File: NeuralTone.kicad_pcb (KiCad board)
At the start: 2 copper layers, 90 parts, among them J1 Power Port (5V@3A), J2 Guitar, J3 Headphone, J4 USB Port, J5 Line Out, J6 TF-01A, J7 RPi CM4Lite Compatible, J8 RPi CM4Lite Compatible, SW1 SW_Push, U1 MCP6022, U2 LDLN025M33R, U3 LDLN025M33R, U4 AP2151, U5 NAU8814YG, Y1 DSB211SDN 26MHz

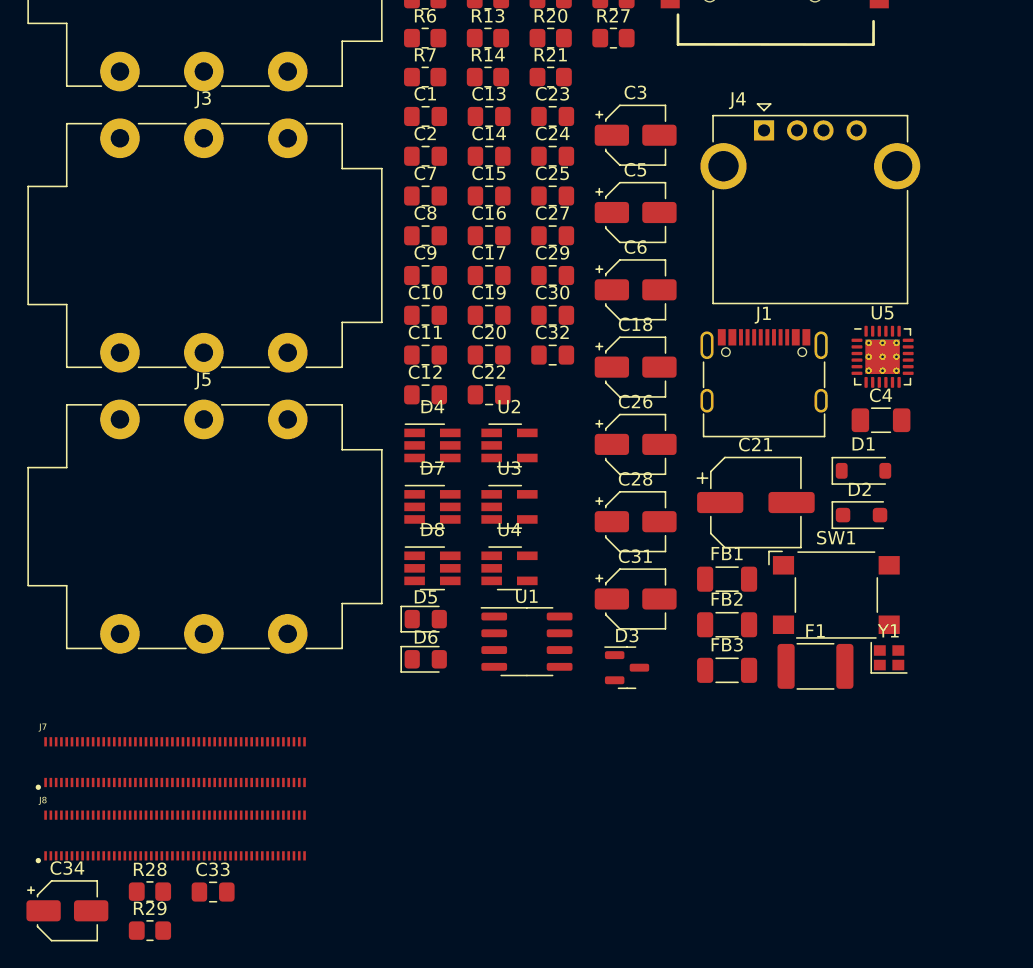
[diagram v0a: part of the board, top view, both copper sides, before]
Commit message: better decoupling strategy
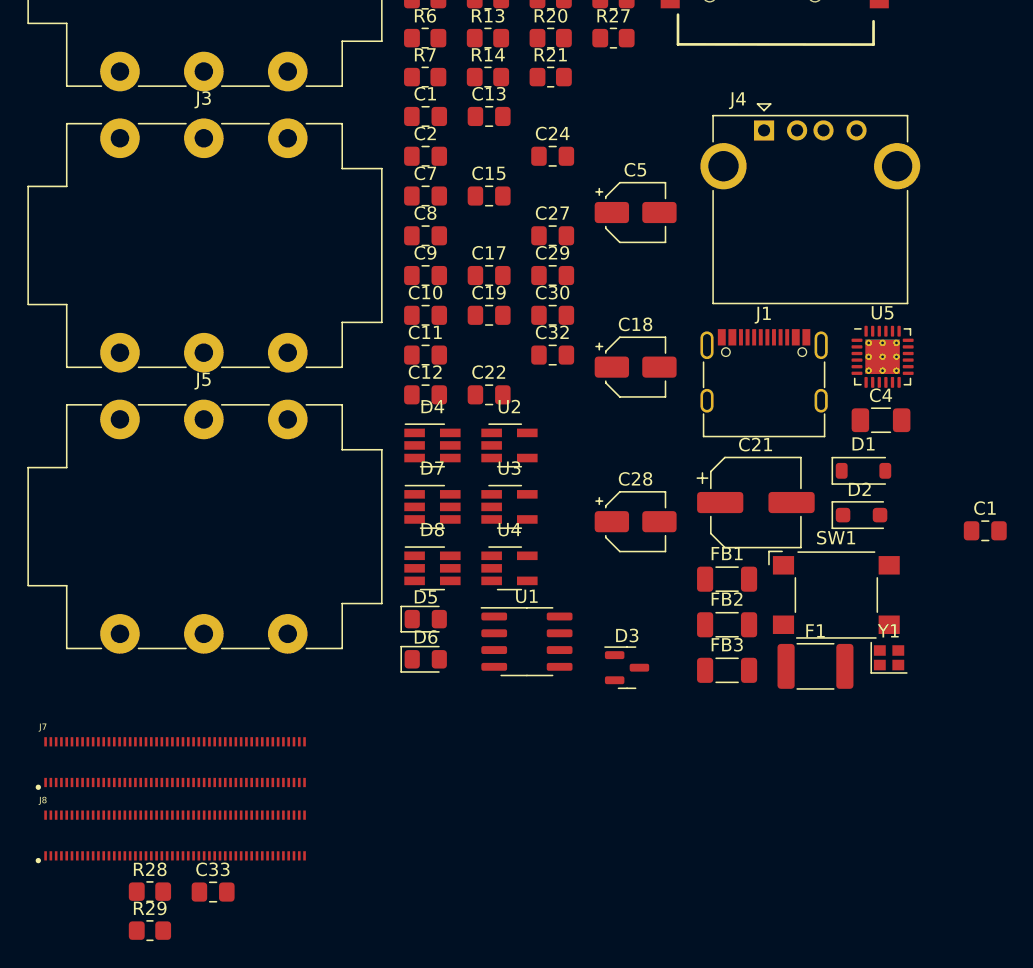
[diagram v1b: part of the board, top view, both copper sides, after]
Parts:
- removed C14, C16, C20, C23, C25: 100n, Capacitor_SMD:C_0805_2012Metric_Pad1.18x1.45mm_HandSolder
- removed C26, C31: 10u, Capacitor_SMD:CP_Elec_4x5.4
- removed C3, C34, C6: 4.7u, Capacitor_SMD:CP_Elec_4x5.4
- added C1: 4.7u, Capacitor_SMD:C_0805_2012Metric_Pad1.18x1.45mm_HandSolder, F.Cu at (186.9, 106.7)
- C1: value 10n -> 4.7u
- C10, C11, C12, C9: value 1u -> 4.7u
- C2: value 100n -> 4.7u
- C27, C30, C32, C33, C7, C8: value 100n -> 470n
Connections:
- C1 pad 1: Net-(D2-K) -> +5V
- C32 pad 1: Net-(J6-CLK) -> +3V3

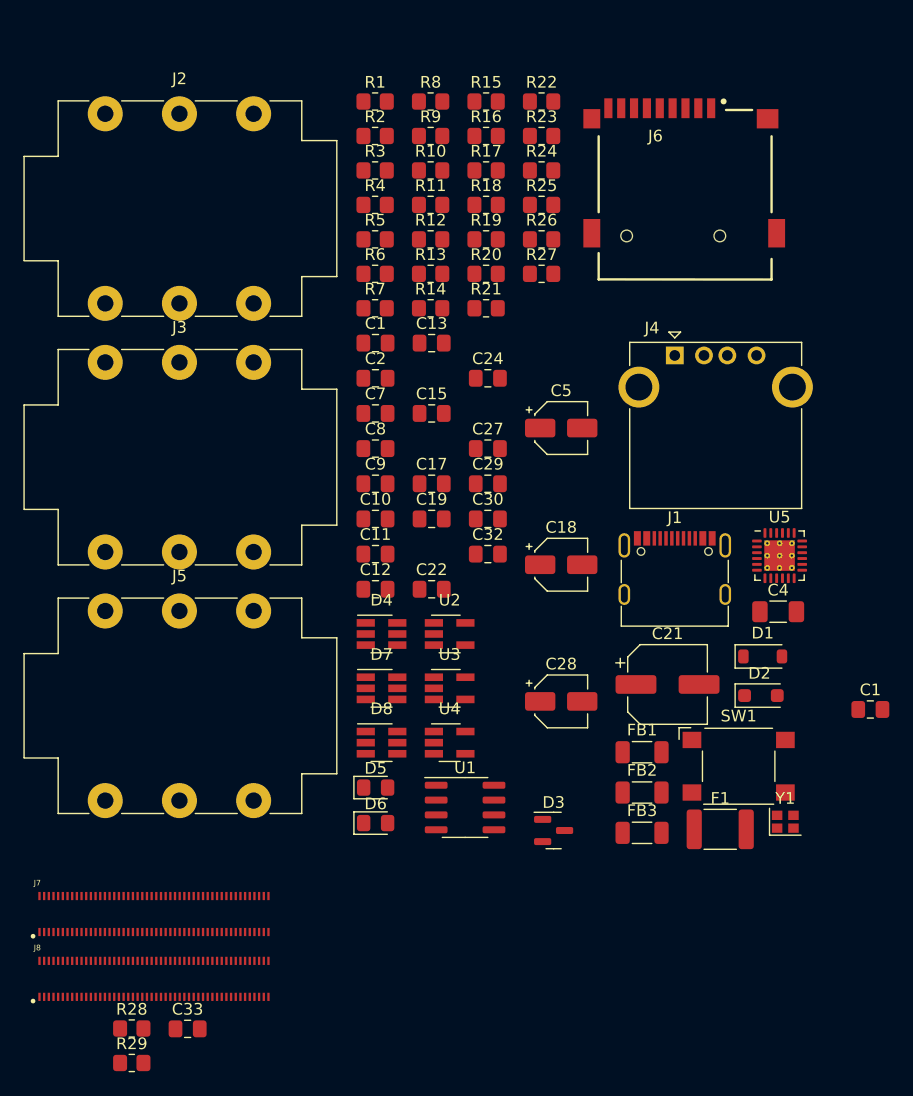
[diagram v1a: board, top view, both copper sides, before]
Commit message: update to a proper USB PD chip
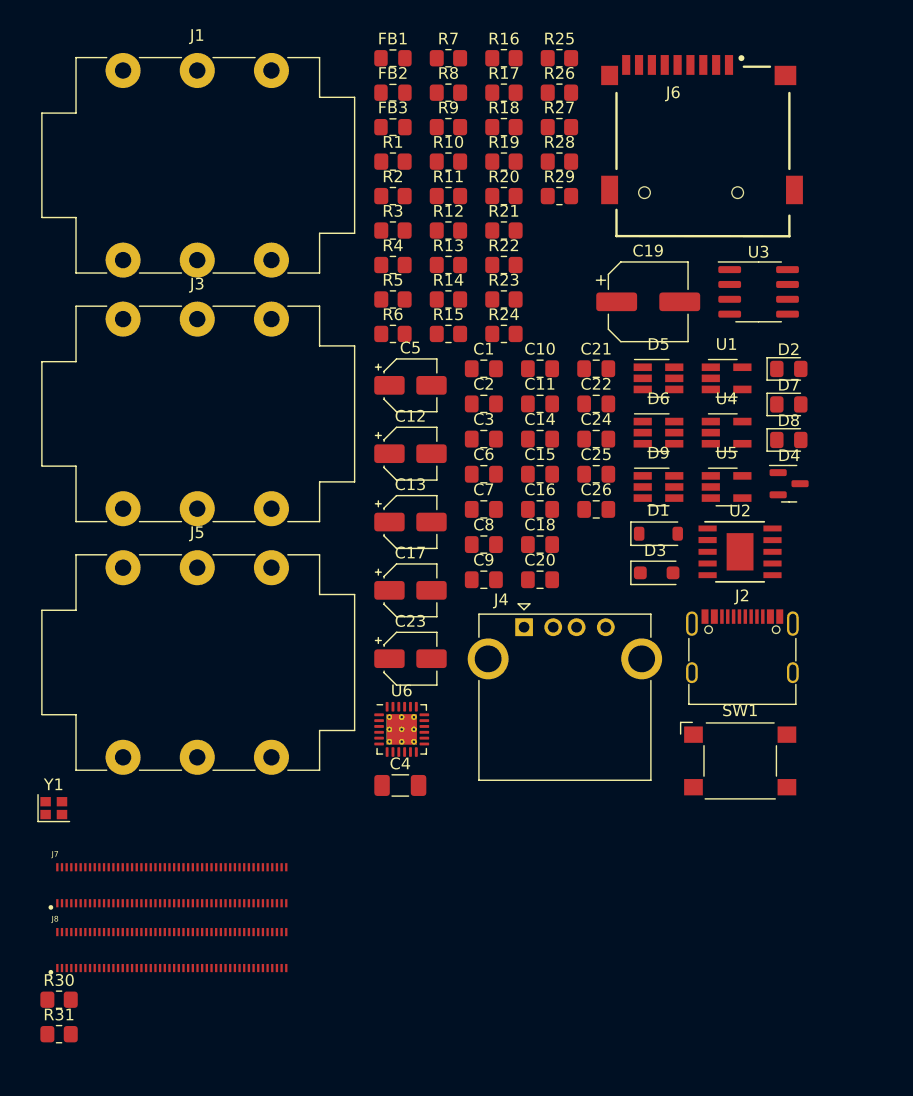
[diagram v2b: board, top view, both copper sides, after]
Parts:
- removed the C1 at (186.9, 106.7)
- removed the C1 at (144.6, 75.3)
- removed C27, C30, C32, C33: 470n, Capacitor_SMD:C_0805_2012Metric_Pad1.18x1.45mm_HandSolder
- removed C28: 10u, Capacitor_SMD:CP_Elec_4x5.4
- removed C29: 100p, Capacitor_SMD:C_0805_2012Metric_Pad1.18x1.45mm_HandSolder
- removed F1: 1812L300, Fuse:Fuse_1812_4532Metric_Pad1.30x3.40mm_HandSolder
- added C1: 1u, Capacitor_SMD:C_0805_2012Metric_Pad1.18x1.45mm_HandSolder, F.Cu at (153.8, 77.5)
- added C14: 4.7u, Capacitor_SMD:C_0805_2012Metric_Pad1.18x1.45mm_HandSolder, F.Cu at (158.6, 83.5)
- added C16: 100p, Capacitor_SMD:C_0805_2012Metric_Pad1.18x1.45mm_HandSolder, F.Cu at (158.6, 89.6)
- added C20: 4.7u, Capacitor_SMD:C_0805_2012Metric_Pad1.18x1.45mm_HandSolder, F.Cu at (158.6, 95.6)
- added C23: 4.7u, Capacitor_SMD:CP_Elec_4x5.4, F.Cu at (147.6, 102.3)
- added C25: 470n, Capacitor_SMD:C_0805_2012Metric_Pad1.18x1.45mm_HandSolder, F.Cu at (163.5, 86.5)
- added C26: 4.7u, Capacitor_SMD:C_0805_2012Metric_Pad1.18x1.45mm_HandSolder, F.Cu at (163.5, 89.6)
- added C3: 1u, Capacitor_SMD:C_0805_2012Metric_Pad1.18x1.45mm_HandSolder, F.Cu at (153.8, 83.5)
- added C6: 4.7u, Capacitor_SMD:C_0805_2012Metric_Pad1.18x1.45mm_HandSolder, F.Cu at (153.8, 86.5)
- added D9: PESD3V3S4UD, Package_TO_SOT_SMD:SOT-23-6_Handsoldering, F.Cu at (168.8, 87.6)
- added R30: 330, Resistor_SMD:R_0805_2012Metric_Pad1.20x1.40mm_HandSolder, F.Cu at (117.5, 131.5)
- added R31: 330, Resistor_SMD:R_0805_2012Metric_Pad1.20x1.40mm_HandSolder, F.Cu at (117.5, 134.5)
- added U6: NAU8814YG, Package_DFN_QFN:QFN-24-1EP_4x4mm_P0.5mm_EP2.6x2.6mm_ThermalVias, F.Cu at (146.8, 108.4)
- C10, C11: value 4.7u -> 10n
- C12, C13: value 4.7u -> 22u; footprint Capacitor_SMD:C_0805_2012Metric_Pad1.18x1.45mm_HandSolder -> Capacitor_SMD:CP_Elec_4x5.4
- C17: value 100p -> 22u; footprint Capacitor_SMD:C_0805_2012Metric_Pad1.18x1.45mm_HandSolder -> Capacitor_SMD:CP_Elec_4x5.4
- C18: value 10u -> 4.7u; footprint Capacitor_SMD:CP_Elec_4x5.4 -> Capacitor_SMD:C_0805_2012Metric_Pad1.18x1.45mm_HandSolder
- C19: value 4.7u -> 150u; footprint Capacitor_SMD:C_0805_2012Metric_Pad1.18x1.45mm_HandSolder -> Capacitor_SMD:CP_Elec_6.3x5.8
- C21: value 100u -> 4.7u; footprint Capacitor_SMD:CP_Elec_6.3x7.7 -> Capacitor_SMD:C_0805_2012Metric_Pad1.18x1.45mm_HandSolder
- C24: value 4.7u -> 100p
- C4: value 150n -> 100n
- C7: value 470n -> 1u
- C9: value 4.7u -> 470n
- D2: value SMF6.0A -> LED_Small; footprint Diode_SMD:D_SOD-123F -> LED_SMD:LED_0805_2012Metric_Pad1.15x1.40mm_HandSolder
- D3: value PESD5V2S2UT -> SMF5.0A; footprint Package_TO_SOT_SMD:SOT-23 -> Diode_SMD:D_SOD-123F
- D4: value PESD3V3S4UD -> PESD5V2S2UT; footprint Package_TO_SOT_SMD:SOT-23-6_Handsoldering -> Package_TO_SOT_SMD:SOT-23
- D5: value LED_Small -> USBLC6-2P6; footprint LED_SMD:LED_0805_2012Metric_Pad1.15x1.40mm_HandSolder -> Package_TO_SOT_SMD:SOT-23-6_Handsoldering
- D6: value LED_Small -> PESD3V3S4UD; footprint LED_SMD:LED_0805_2012Metric_Pad1.15x1.40mm_HandSolder -> Package_TO_SOT_SMD:SOT-23-6_Handsoldering
- D7: value PESD3V3S4UD -> LED_Small; footprint Package_TO_SOT_SMD:SOT-23-6_Handsoldering -> LED_SMD:LED_0805_2012Metric_Pad1.15x1.40mm_HandSolder
- D8: value USBLC6-2P6 -> LED_Small; footprint Package_TO_SOT_SMD:SOT-23-6_Handsoldering -> LED_SMD:LED_0805_2012Metric_Pad1.15x1.40mm_HandSolder
- FB1: value BLM31PG121SN1L -> BLM21PG220SN1; footprint Inductor_SMD:L_1206_3216Metric_Pad1.22x1.90mm_HandSolder -> Inductor_SMD:L_0805_2012Metric_Pad1.15x1.40mm_HandSolder
- FB2, FB3: value BLM31PG121SN1L -> BLM21AG102SN1; footprint Inductor_SMD:L_1206_3216Metric_Pad1.22x1.90mm_HandSolder -> Inductor_SMD:L_0805_2012Metric_Pad1.15x1.40mm_HandSolder
- J1: value Power Port (5V@3A) -> Guitar; footprint Connector_USB:USB_C_Receptacle_G-Switch_GT-USB-7010ASV -> Connector_Audio:Jack_6.35mm_Neutrik_NMJ6HCD2_Horizontal
- J2: value Guitar -> 5V@3A; footprint Connector_Audio:Jack_6.35mm_Neutrik_NMJ6HCD2_Horizontal -> Connector_USB:USB_C_Receptacle_G-Switch_GT-USB-7010ASV
- J3: value Headphone -> Headphones
- R1: value 1.8k -> 1k
- R11: value 10k -> 2.2M
- R14, R15, R20: value 22 -> 10k
- R18, R19: value 10k -> 22
- R2: value 3.9k -> 10k
- R21: value 330 -> 10k
- R23, R26: value 22 -> 1k
- R24, R28, R29: value 330 -> 22
- R3: value 5.1k -> 10k
- R4: value 100 -> 10k
- R5: value 5.1k -> 1.8k
- R6: value 2.2M -> 3.9k
- R7: value 10k -> 100
- R9: value 10k -> 1k
- U1: value MCP6022 -> LDLN025M33R; footprint Package_SO:SOIC-8_3.9x4.9mm_P1.27mm -> Package_TO_SOT_SMD:SOT-23-5_HandSoldering
- U2: value LDLN025M33R -> CH224K; footprint Package_TO_SOT_SMD:SOT-23-5_HandSoldering -> NeuralTone:CH224K
- U3: value LDLN025M33R -> MCP6022; footprint Package_TO_SOT_SMD:SOT-23-5_HandSoldering -> Package_SO:SOIC-8_3.9x4.9mm_P1.27mm
- U4: value AP2151 -> LDLN025M33R
- U5: value NAU8814YG -> AP2151; footprint Package_DFN_QFN:QFN-24-1EP_4x4mm_P0.5mm_EP2.6x2.6mm_ThermalVias -> Package_TO_SOT_SMD:SOT-23-5_HandSoldering
- moved R28 82.7 mm to (160.3, 59.8)
- moved R29 82.7 mm to (160.3, 62.7)
- moved J2 71.8 mm to (176.0, 102.5)
- moved J1 64.4 mm to (123.0, 52.0)
- moved FB3 64.1 mm to (146.1, 56.8)
- moved FB2 63.6 mm to (146.1, 53.9)
- moved FB1 63.1 mm to (146.1, 50.9)
- moved Y1 62.6 mm to (117.0, 115.1)
- moved D8 43.4 mm to (179.9, 83.6)
- moved U3 43.0 mm to (177.4, 70.9)
- moved U1 43.0 mm to (174.6, 78.3)
- moved D5 42.6 mm to (168.8, 78.3)
- moved D7 42.5 mm to (179.9, 80.6)
- moved D6 41.3 mm to (168.8, 83.0)
- moved D4 37.2 mm to (180.0, 87.4)
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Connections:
- C10 pad 1: +3V3A_C -> /VBUS
- C13 pad 1: +3V3A_C -> +5V
- C17 pad 1: Net-(C17-Pad1) -> /HEADPHONES
- C17 pad 2: GND -> Net-(C16-Pad1)
- C18 pad 1: /HEADPHONE -> GND
- C18 pad 2: Net-(C17-Pad1) -> Net-(U6-VREF)
- C19 pad 1: GND -> Net-(J4-VBUS)
- C19 pad 2: Net-(U5-VREF) -> GND
- C2 pad 1: +5V -> +3V3A_B
- C21 pad 1: Net-(J4-VBUS) -> +3V3
- C22 pad 1: +3V3 -> +5V
- C24 pad 1: +3V3 -> GND
- C24 pad 2: GND -> Net-(C23-Pad2)
- C4 pad 2: Net-(U1B-+) -> Net-(U3B-+)
- C5 pad 1: Net-(U1B--) -> Net-(U3B--)
- C7 pad 1: GND -> +5V
- C7 pad 2: Net-(U1A-+) -> GND
- C8 pad 2: +3V3A_B -> Net-(U3A-+)
- C9 pad 1: +3V3A_B -> GND
- C9 pad 2: GND -> +3V3A_B
- D2 pad 2: GND -> Net-(D2-A)
- D3 pad 1: Net-(C17-Pad1) -> /VBUS
- D3 pad 2: Net-(C28-Pad2) -> GND
- D4 pad 1: Net-(J6-DAT2) -> Net-(C16-Pad1)
- D4 pad 2: GND -> Net-(C23-Pad2)
- D4 pad 3: Net-(J6-DAT3/CD) -> GND
- D5 pad 1: GND -> USBD+
- D5 pad 2: Net-(D5-A) -> GND
- D6 pad 1: GND -> Net-(J6-DAT2)
- D6 pad 2: Net-(D6-A) -> GND
- D7 pad 1: Net-(J6-CLK) -> GND
- D7 pad 2: GND -> Net-(D7-A)
- D8 pad 1: USBD+ -> GND
- D8 pad 2: GND -> Net-(D8-A)
- FB1 pad 1: Net-(D2-K) -> /VBUS
- FB2 pad 1: Net-(C17-Pad1) -> Net-(C16-Pad1)
- FB3 pad 1: Net-(C28-Pad2) -> Net-(C23-Pad2)
- R1 pad 1: Net-(J2-PadT) -> /VBUS
- R1 pad 2: Net-(D1-A) -> /VDD
- R10 pad 2: Net-(U1A-+) -> Net-(C5-Pad2)
- R11 pad 1: +5V -> Net-(U3A--)
- R11 pad 2: Net-(U2-EN) -> Net-(U3B-+)
- R12 pad 1: +5V -> Net-(U3A-+)
- R12 pad 2: Net-(U3-EN) -> +3V3A_B
- R14 pad 1: I2S_DOUT -> GND
- R14 pad 2: Net-(U5-ADCOUT) -> Net-(U3A-+)
- R15 pad 1: I2S_DIN -> +5V
- R15 pad 2: Net-(U5-DACIN) -> Net-(U5-EN)
- R16 pad 1: I2S_LRCK -> I2S_DOUT
- R16 pad 2: Net-(U5-FS) -> Net-(U6-ADCOUT)
- R17 pad 1: I2S_BCK -> I2S_DIN
- R17 pad 2: Net-(U5-BCLK) -> Net-(U6-DACIN)
- R18 pad 1: Net-(U5-MODE) -> I2S_LRCK
- R18 pad 2: GND -> Net-(U6-FS)
- R19 pad 1: GND -> I2S_BCK
- R19 pad 2: Net-(U5-CSb/GPIO) -> Net-(U6-BCLK)
- R2 pad 1: Net-(D1-A) -> +5V
- R2 pad 2: Net-(C4-Pad1) -> Net-(U1-EN)
- R20 pad 1: SD_DAT2 -> Net-(U6-MODE)
- R20 pad 2: Net-(J6-DAT2) -> GND
- R21 pad 1: LED_STAT_1 -> GND
- R21 pad 2: Net-(D5-A) -> Net-(U6-CSb/GPIO)
- R22 pad 1: SD_DAT3 -> SD_DAT2
- R22 pad 2: Net-(J6-DAT3/CD) -> Net-(J6-DAT2)
- R23 pad 1: SD_CMD -> LED_STAT_1
- R23 pad 2: Net-(J6-CMD) -> Net-(D7-A)
- R24 pad 1: LED_STAT_2 -> SD_DAT3
- R24 pad 2: Net-(D6-A) -> Net-(J6-DAT3/CD)
- R25 pad 1: SD_CLK -> SD_CMD
- R25 pad 2: Net-(J6-CLK) -> Net-(J6-CMD)
- R26 pad 1: SD_DAT0 -> LED_STAT_2
- R26 pad 2: Net-(J6-DAT0) -> Net-(D8-A)
- R27 pad 1: SD_DAT1 -> SD_CLK
- R27 pad 2: Net-(J6-DAT1) -> Net-(J6-CLK)
- R28 pad 1: I2C_SCL -> SD_DAT0
- R28 pad 2: Net-(J7-GPIO3) -> Net-(J6-DAT0)
- R29 pad 1: I2C_SDA -> SD_DAT1
- R29 pad 2: Net-(J7-GPIO2) -> Net-(J6-DAT1)
- R3 pad 1: Net-(J1-CC1) -> /VBUS
- R3 pad 2: GND -> Net-(U2-VBUS)
- R4 pad 1: Net-(C5-Pad2) -> Net-(U2-CFG1)
- R4 pad 2: CODEC_AUX -> /VDD
- R5 pad 1: Net-(J1-CC2) -> Net-(J1-PadT)
- R5 pad 2: GND -> Net-(D1-A)
- R6 pad 1: Net-(C4-Pad1) -> Net-(D1-A)
- R6 pad 2: GND -> Net-(C4-Pad1)
- R7 pad 1: GND -> Net-(C5-Pad2)
- R7 pad 2: Net-(C5-Pad2) -> CODEC_AUX
- R8 pad 1: Net-(U1A--) -> Net-(C4-Pad1)
- R8 pad 2: Net-(U1B-+) -> GND
- R9 pad 1: Net-(U1A-+) -> Net-(D2-A)
- R9 pad 2: +3V3A_B -> /VDD
- U1 pad 1: Net-(U1A--) -> +5V
- U1 pad 2: Net-(U1A--) -> GND
- U1 pad 3: Net-(U1A-+) -> Net-(U1-EN)
- U1 pad 4: GND -> unconnected-(U1-NC-Pad4)
- U1 pad 5: Net-(U1B-+) -> +3V3A_B
- U2 pad 1: +5V -> /VDD
- U2 pad 2: GND -> unconnected-(U2-CFG2-Pad2)
- U2 pad 3: Net-(U2-EN) -> unconnected-(U2-CFG3-Pad3)
- U2 pad 4: unconnected-(U2-NC-Pad4) -> Net-(U2-DP)
- U2 pad 5: +3V3A_B -> Net-(U2-DM)
- U3 pad 1: +5V -> Net-(U3A--)
- U3 pad 2: GND -> Net-(U3A--)
- U3 pad 3: Net-(U3-EN) -> Net-(U3A-+)
- U3 pad 4: unconnected-(U3-NC-Pad4) -> GND
- U3 pad 5: +3V3A_C -> Net-(U3B-+)
- U4 pad 1: Net-(J4-VBUS) -> +5V
- U4 pad 3: unconnected-(U4-~{FLG}-Pad3) -> Net-(U4-EN)
- U4 pad 4: Net-(U4-EN) -> unconnected-(U4-NC-Pad4)
- U4 pad 5: +5V -> +3V3A_C
- U5 pad 1: unconnected-(U5-MICBIAS-Pad1) -> Net-(J4-VBUS)
- U5 pad 2: +3V3A_C -> GND
- U5 pad 3: GND -> unconnected-(U5-~{FLG}-Pad3)
- U5 pad 4: +3V3 -> Net-(U5-EN)
- U5 pad 5: +3V3 -> +5V

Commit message: cleanup and lcsc part numbers
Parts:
- removed FB3: BLM21AG102SN1, Inductor_SMD:L_0805_2012Metric_Pad1.15x1.40mm_HandSolder
- added C27: 4.7u, Capacitor_SMD:C_0805_2012Metric_Pad1.18x1.45mm_HandSolder, F.Cu at (180.7, 87.5)
- added L1: 104CDMCCDS 4.7u, NeuralTone:104CDMCC_DS, F.Cu at (152.5, 96.5)
- added Q1: AON7421, NeuralTone:DMP2008UFG, F.Cu at (134.0, 113.8)
- added R32: 330, Resistor_SMD:R_0805_2012Metric_Pad1.20x1.40mm_HandSolder, F.Cu at (119.0, 135.2)
- added U7: DRTR5V0U2SR, Package_TO_SOT_SMD:SOT-143_Handsoldering, F.Cu at (162.9, 114.6)
- C10: value 10n -> 100n
- C11: value 10n -> 47u; footprint Capacitor_SMD:C_0805_2012Metric_Pad1.18x1.45mm_HandSolder -> Capacitor_SMD:C_1210_3225Metric_Pad1.33x2.70mm_HandSolder
- C12: value 22u -> 47u; footprint Capacitor_SMD:CP_Elec_4x5.4 -> Capacitor_SMD:C_1210_3225Metric_Pad1.33x2.70mm_HandSolder
- C13: value 22u -> 4.7u; footprint Capacitor_SMD:CP_Elec_4x5.4 -> Capacitor_SMD:C_0805_2012Metric_Pad1.18x1.45mm_HandSolder
- C15: value 4.7u -> 470u; footprint Capacitor_SMD:C_0805_2012Metric_Pad1.18x1.45mm_HandSolder -> Capacitor_SMD:CP_Elec_10x10
- C16, C24: value 100p -> 33p
- C17: value 22u -> 33p; footprint Capacitor_SMD:CP_Elec_4x5.4 -> Capacitor_SMD:C_0805_2012Metric_Pad1.18x1.45mm_HandSolder
- C19: footprint Capacitor_SMD:CP_Elec_6.3x5.8 -> Capacitor_SMD:CP_Elec_6.3x7.7
- C2, C6: value 4.7u -> 1u
- C23, C5: footprint Capacitor_SMD:CP_Elec_4x5.4 -> Capacitor_SMD:CP_Elec_4x5.3
- C25: value 470n -> 33p
- C26: value 4.7u -> 100n
- C8: value 470n -> 4.7u
- C9: value 470n -> 1u
- D2: value LED_Small -> SMF5.0A; footprint LED_SMD:LED_0805_2012Metric_Pad1.15x1.40mm_HandSolder -> Diode_SMD:D_SOD-123F
- D3: value SMF5.0A -> LED_Small; footprint Diode_SMD:D_SOD-123F -> LED_SMD:LED_1206_3216Metric_Pad1.42x1.75mm_HandSolder
- D4: value PESD5V2S2UT -> SMF5.0CA; footprint Package_TO_SOT_SMD:SOT-23 -> Diode_SMD:D_SOD-123F
- D5: value USBLC6-2P6 -> SMF5.0CA; footprint Package_TO_SOT_SMD:SOT-23-6_Handsoldering -> Diode_SMD:D_SOD-123F
- D7, D8: footprint LED_SMD:LED_0805_2012Metric_Pad1.15x1.40mm_HandSolder -> LED_SMD:LED_1206_3216Metric_Pad1.42x1.75mm_HandSolder
- FB2: value BLM21AG102SN1 -> BLM21PG220SN1
- J1: value Guitar -> USB C; footprint Connector_Audio:Jack_6.35mm_Neutrik_NMJ6HCD2_Horizontal -> Connector_USB:USB_C_Receptacle_G-Switch_GT-USB-7010ASV
- J2: value 5V@3A -> Guitar; footprint Connector_USB:USB_C_Receptacle_G-Switch_GT-USB-7010ASV -> Connector_Audio:Jack_6.35mm_Neutrik_NMJ6HCD2_Horizontal
- J7, J8: value RPi CM4Lite Compatible -> DF40HC(3.0)-100DS
- R10: value 10k -> 220m
- R11: value 2.2M -> 220m
- R12, R13: value 10k -> 1k
- R14, R3: value 10k -> 1.8k
- R22: value 22 -> 10k
- R23, R26: value 1k -> 22
- R24, R27: value 22 -> 1k
- R30: value 330 -> 22
- R4: value 10k -> 3.9k
- R5: value 1.8k -> 10k
- R6: value 3.9k -> 2.2M
- R7: value 100 -> 10k
- R8: value 2.2M -> 10k
- U1, U4: value LDLN025M33R -> AP2125N-3.3; footprint Package_TO_SOT_SMD:SOT-23-5_HandSoldering -> Package_TO_SOT_SMD:SOT-23
- Y1: value DSB211SDN 26MHz -> OT322512MJBA4SL; footprint Crystal:Crystal_SMD_2016-4Pin_2.0x1.6mm -> Crystal:Crystal_SMD_3225-4Pin_3.2x2.5mm
- moved R30 83.6 mm to (161.8, 60.7)
- moved J2 73.6 mm to (124.5, 49.9)
- moved U3 71.4 mm to (120.8, 114.5)
- moved J1 66.9 mm to (173.4, 95.9)
- moved Y1 53.2 mm to (170.2, 112.1)
- moved U5 43.7 mm to (139.4, 113.6)
- moved C19 43.2 mm to (178.6, 113.6)
- moved SW1 41.9 mm to (169.8, 69.6)
- moved C12 40.4 mm to (181.3, 107.0)
- moved C17 33.6 mm to (175.9, 78.5)
- moved D8 32.1 mm to (162.8, 110.7)
- moved D7 31.8 mm to (162.8, 107.3)
- moved C11 31.7 mm to (181.3, 102.7)
- moved D1 28.4 mm to (154.1, 116.0)
- moved U2 24.6 mm to (179.5, 68.9)
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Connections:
- C10 pad 1: /VBUS -> GND
- C10 pad 2: GND -> +3V3A_B
- C11 pad 1: +5V -> Net-(C11-Pad1)
- C12 pad 1: +5V -> Net-(C12-Pad1)
- C13 pad 1: +5V -> +3V3A_C
- C15 pad 1: +3V3A_C -> /HEADPHONES
- C15 pad 2: GND -> Net-(C15-Pad2)
- C16 pad 1: Net-(C16-Pad1) -> GND
- C16 pad 2: GND -> Net-(C15-Pad2)
- C17 pad 1: /HEADPHONES -> GND
- C17 pad 2: Net-(C16-Pad1) -> Net-(C17-Pad2)
- C2 pad 1: +3V3A_B -> +5V
- C25 pad 1: +3V3 -> GND
- C25 pad 2: GND -> Net-(C25-Pad2)
- C3 pad 1: +5V -> +3V3A_B
- C5 pad 2: Net-(C5-Pad2) -> CODEC_AUX
- C6 pad 1: +3V3A_C -> +5V
- C7 pad 1: +5V -> +3V3A_C
- C9 pad 1: GND -> Net-(Q1-D)
- C9 pad 2: +3V3A_B -> Net-(Q1-G)
- D2 pad 1: Net-(D2-K) -> /VBUS
- D2 pad 2: Net-(D2-A) -> GND
- D3 pad 1: /VBUS -> GND
- D3 pad 2: GND -> Net-(D3-A)
- D4 pad 1: Net-(C16-Pad1) -> GND
- D4 pad 2: Net-(C23-Pad2) -> Net-(C17-Pad2)
- D5 pad 1: USBD+ -> GND
- D5 pad 2: GND -> Net-(C25-Pad2)
- FB1 pad 1: /VBUS -> Net-(C15-Pad2)
- FB1 pad 2: +5V -> Net-(C17-Pad2)
- FB2 pad 1: Net-(C16-Pad1) -> Net-(C23-Pad2)
- FB2 pad 2: Net-(FB2-Pad2) -> Net-(C25-Pad2)
- J3 pad R: Net-(FB2-Pad2) -> Net-(C17-Pad2)
- J3 pad T: Net-(FB2-Pad2) -> Net-(C17-Pad2)
- J4 pad 2: Net-(J4-D-) -> USBD-
- J4 pad 3: Net-(J4-D+) -> USBD+
- J5 pad R: Net-(FB3-Pad2) -> Net-(C25-Pad2)
- J5 pad T: Net-(FB3-Pad2) -> Net-(C25-Pad2)
- R10 pad 1: GND -> Net-(Q1-D)
- R10 pad 2: Net-(C5-Pad2) -> Net-(C11-Pad1)
- R11 pad 1: Net-(U3A--) -> +5V
- R11 pad 2: Net-(U3B-+) -> Net-(C12-Pad1)
- R12 pad 1: Net-(U3A-+) -> +5V
- R12 pad 2: +3V3A_B -> Net-(D3-A)
- R13 pad 1: +5V -> Net-(Q1-G)
- R13 pad 2: Net-(U4-EN) -> /PG
- R14 pad 1: GND -> Net-(C15-Pad2)
- R14 pad 2: Net-(U3A-+) -> GND
- R2 pad 1: +5V -> Net-(U2-CFG1)
- R2 pad 2: Net-(U1-EN) -> /VDD
- R21 pad 1: GND -> Net-(C23-Pad2)
- R21 pad 2: Net-(U6-CSb/GPIO) -> GND
- R22 pad 1: SD_DAT2 -> GND
- R22 pad 2: Net-(J6-DAT2) -> Net-(U6-CSb/GPIO)
- R23 pad 1: LED_STAT_1 -> SD_DAT2
- R23 pad 2: Net-(D7-A) -> Net-(J6-DAT2)
- R24 pad 1: SD_DAT3 -> LED_STAT_1
- R24 pad 2: Net-(J6-DAT3/CD) -> Net-(D7-A)
- R25 pad 1: SD_CMD -> SD_DAT3
- R25 pad 2: Net-(J6-CMD) -> Net-(J6-DAT3/CD)
- R26 pad 1: LED_STAT_2 -> SD_CMD
- R26 pad 2: Net-(D8-A) -> Net-(J6-CMD)
- R27 pad 1: SD_CLK -> LED_STAT_2
- R27 pad 2: Net-(J6-CLK) -> Net-(D8-A)
- R28 pad 1: SD_DAT0 -> SD_CLK
- R28 pad 2: Net-(J6-DAT0) -> Net-(J6-CLK)
- R29 pad 1: SD_DAT1 -> SD_DAT0
- R29 pad 2: Net-(J6-DAT1) -> Net-(J6-DAT0)
- R3 pad 1: /VBUS -> Net-(J2-PadT)
- R3 pad 2: Net-(U2-VBUS) -> Net-(D1-A)
- R30 pad 1: I2C_SCL -> SD_DAT1
- R30 pad 2: Net-(J7-GPIO3) -> Net-(J6-DAT1)
- R31 pad 1: I2C_SDA -> I2C_SCL
- R31 pad 2: Net-(J7-GPIO2) -> Net-(J7-GPIO3)
- R4 pad 1: Net-(U2-CFG1) -> Net-(D1-A)
- R4 pad 2: /VDD -> Net-(C4-Pad1)
- R5 pad 1: Net-(J1-PadT) -> GND
- R5 pad 2: Net-(D1-A) -> CODEC_AUX
- R6 pad 1: Net-(D1-A) -> Net-(U3A--)
- R6 pad 2: Net-(C4-Pad1) -> Net-(U3B-+)
- R7 pad 1: Net-(C5-Pad2) -> Net-(U3A-+)
- R7 pad 2: CODEC_AUX -> +3V3A_B
- R8 pad 1: Net-(C4-Pad1) -> GND
- R8 pad 2: GND -> Net-(U3A-+)
- R9 pad 1: Net-(D2-A) -> /VBUS
- R9 pad 2: /VDD -> Net-(Q1-G)
- U1 pad 1: +5V -> GND
- U1 pad 2: GND -> +3V3A_B
- U1 pad 3: Net-(U1-EN) -> +5V
- U2 pad 10: Net-(D2-K) -> /PG
- U2 pad 4: Net-(U2-DP) -> Net-(U2-DM)
- U2 pad 6: Net-(J2-CC2) -> Net-(J1-CC2)
- U2 pad 7: Net-(J2-CC1) -> Net-(J1-CC1)
- U2 pad 8: Net-(U2-VBUS) -> unconnected-(U2-VBUS-Pad8)
- U4 pad 1: +5V -> GND
- U4 pad 2: GND -> +3V3A_C
- U4 pad 3: Net-(U4-EN) -> +5V
- Y1 pad 1: GND -> unconnected-(Y1-Pad1)
